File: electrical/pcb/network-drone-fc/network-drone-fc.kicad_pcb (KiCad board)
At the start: 4 copper layers, 36 x 36 mm, 94 parts, among them J1 U.FL-R-SMT-1, J2 TYPE-C 16PIN 2MD, J3 U.FL GPS, J4 ESC, J5 I2C port, J7 Charging board, U1 ESP32-S3FN8, U2 USBLC6-2SC6, U3 AP63205WU-7, U4 TLV75733PDBVR, U5 TPS7A2033PDBVR, U6 ICM-42688-P, U7 BMP581, U8 MAX-M10S, X1 Q22FA12800101

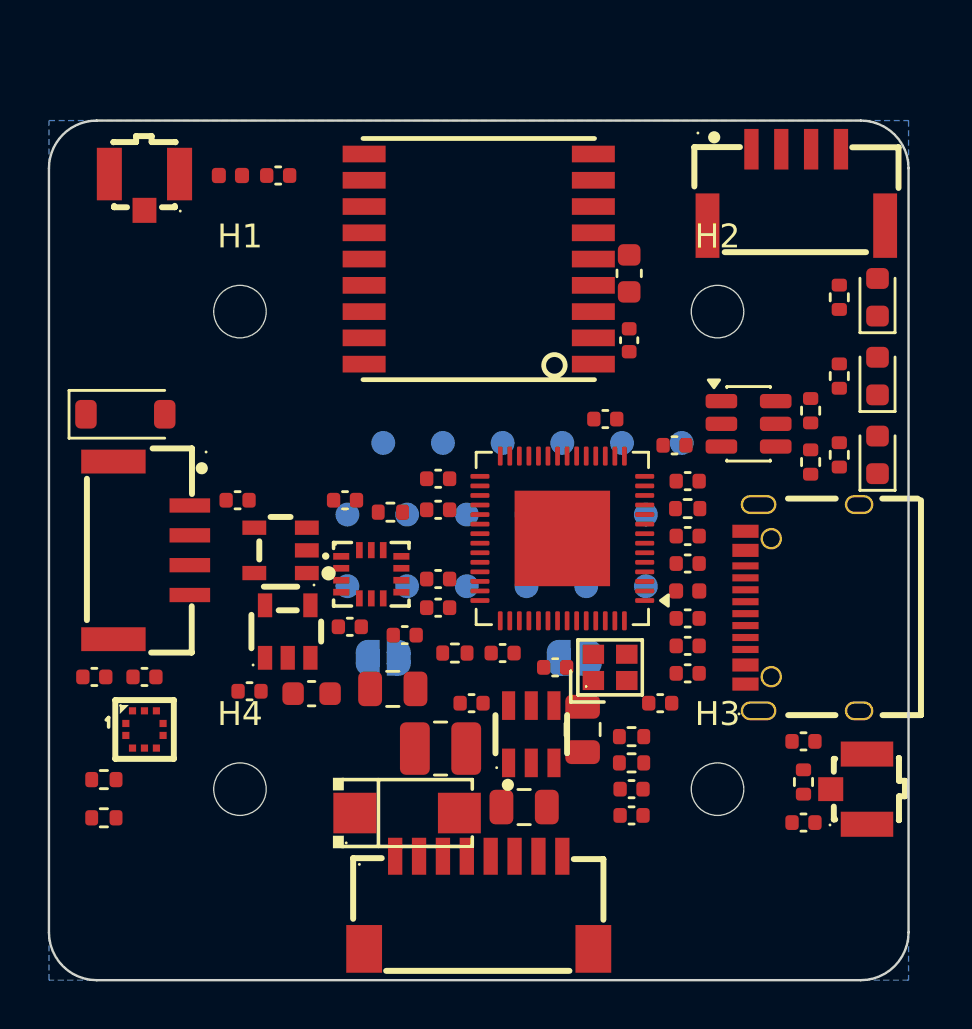
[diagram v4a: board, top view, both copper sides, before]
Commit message: PCB: tighten the buck loop (L2 flipped toward SW, C18 at the inductor output), fix the charging port orientation
The earlier text-level rotation double-rotated J7, L2 and C18 (KiCad stores pad
positions unrotated and applies the footprint angle on load). Corrected, so the
charging port's cable mouth now faces the top edge.
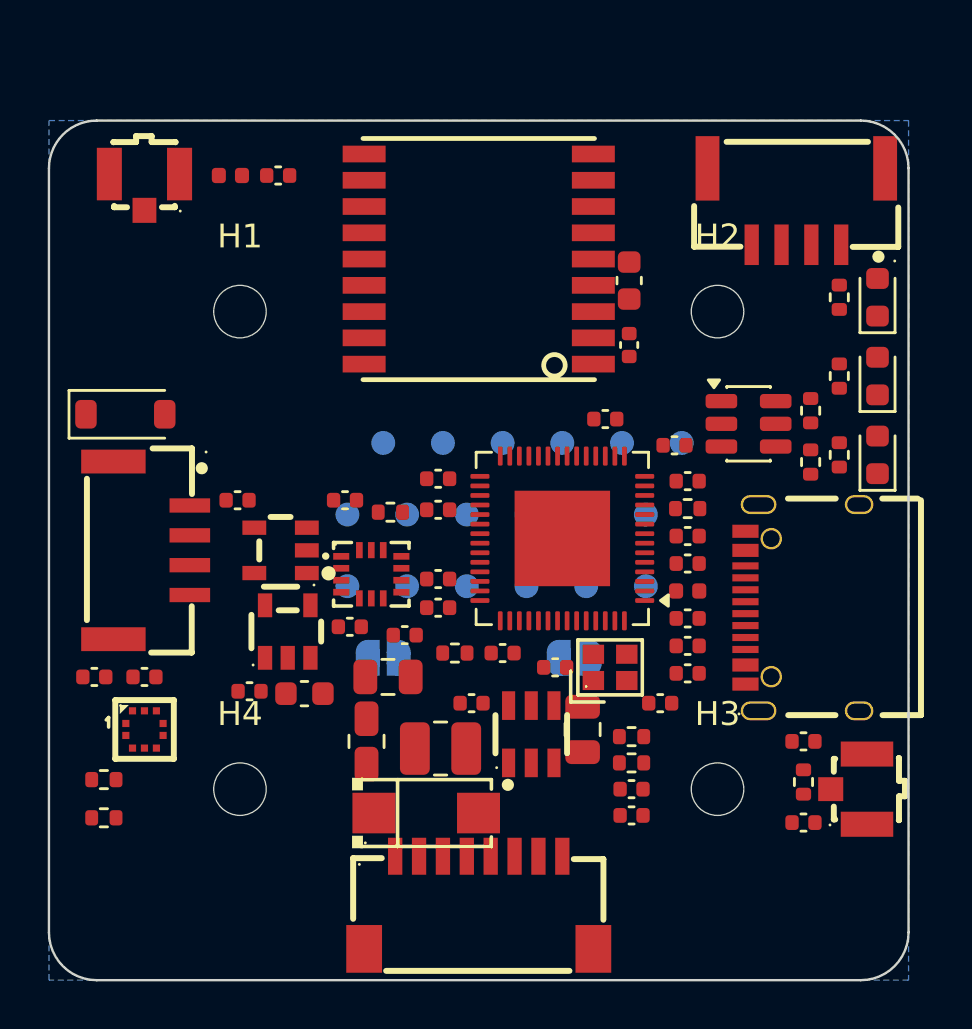
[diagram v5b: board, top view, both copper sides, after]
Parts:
- moved C18 7.15 mm to (95.3, 108.0), turned to 90 degrees
- moved D5 0.80 mm to (97.8, 111.0)
- moved J7 0.80 mm to (113.3, 85.6)
- moved C19 0.54 mm to (96.2, 105.3)
- moved C30 0.30 mm to (106.3, 88.7)
- moved C4 0.30 mm to (92.7, 106.0)
- moved C31 0.20 mm to (106.3, 91.4)
- turned L2 to 180 degrees
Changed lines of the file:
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@@
 	(footprint "SMA_L4.4-W2.6-LS5.0-RD"
 		(layer "F.Cu")
-		(at 97 111)
+		(at 97.8 111.0)
 		(property "Reference" "D5"
 			(at 0 0 0)
@@
 	(footprint "CONN-SMD_4P-P1.25_SM04B-GHS-TB-LF-SN"
 		(layer "F.Cu")
-		(at 113.3 84.8 180)
+		(at 113.3 85.6 180)
 		(property "Reference" "J7"
-			(at 0 0 180)
+			(at -0 0 180)
 			(layer "F.Fab")
 			(effects
@@
 		)
 		(property "Value" "Charging board"
-			(at 0 -5.6 180)
+			(at 0 5.6 180)
 			(layer "F.Fab")
 			(hide yes)
@@
 		)
 		(property "Datasheet" ""
-			(at 0 0 180)
+			(at -0 0 180)
 			(layer "F.Fab")
 			(hide yes)
@@
 		)
 		(property "Description" ""
-			(at 0 0 180)
+			(at -0 0 180)
 			(layer "F.Fab")
 			(hide yes)
@@
 		)
 		(property "LCSC Part" "C189895"
-			(at 0 0 180)
+			(at -0 0 180)
 			(layer "F.Fab")
 			(hide yes)
@@
 		(attr smd)
 		(fp_line
-			(start 4.27 1.69)
-			(end 4.27 0.04)
+			(start -4.27 -1.69)
+			(end -4.27 -0.04)
 			(stroke
 				(width 0.25)
@@
 		)
 		(fp_line
-			(start 3 -2.71)
-			(end -2.92 -2.71)
+			(start -3 2.71)
+			(end 2.92 2.71)
 			(stroke
 				(width 0.25)
@@
 		)
 		(fp_line
-			(start 2.36 1.69)
-			(end 4.27 1.69)
+			(start -2.36 -1.69)
+			(end -4.27 -1.69)
 			(stroke
 				(width 0.25)
@@
 		)
 		(fp_line
-			(start -2.34 1.68)
-			(end -4.28 1.68)
+			(start 2.34 -1.68)
+			(end 4.28 -1.68)
 			(stroke
 				(width 0.25)
@@
 		)
 		(fp_line
-			(start -4.28 1.68)
-			(end -4.28 -0.02)
+			(start 4.28 -1.68)
+			(end 4.28 0.02)
 			(stroke
 				(width 0.25)
@@
 		)
 		(fp_circle
-			(center 4.12 2.28)
-			(end 4.09 2.28)
+			(center -4.12 -2.28)
+			(end -4.09 -2.28)
 			(stroke
 				(width 0.06)
@@
 		)
 		(fp_circle
-			(center 3.44 2.1)
-			(end 3.31 2.1)
+			(center -3.44 -2.1)
+			(end -3.31 -2.1)
 			(stroke
 				(width 0.25)
@@
 		)
 		(fp_circle
-			(center 1.89 1.13)
-			(end 1.76 1.13)
+			(center -1.89 -1.13)
+			(end -1.76 -1.13)
 			(stroke
 				(width 0.25)
@@
 		)
 		(fp_line
-			(start 4.12 1.48)
-			(end -4.13 1.48)
+			(start -4.12 -1.48)
+			(end 4.13 -1.48)
 			(stroke
 				(width 0.05)
@@
 		)
 		(fp_line
-			(start 4.12 -2.57)
-			(end 4.12 1.48)
+			(start -4.12 2.57)
+			(end -4.12 -1.48)
 			(stroke
 				(width 0.05)
@@
 		)
 		(fp_line
-			(start -4.13 1.48)
-			(end -4.13 -2.57)
+			(start 4.13 -1.48)
+			(end 4.13 2.57)
 			(stroke
 				(width 0.05)
@@
 		)
 		(fp_line
-			(start -4.13 -2.57)
-			(end 4.12 -2.57)
+			(start 4.13 2.57)
+			(end -4.12 2.57)
 			(stroke
 				(width 0.05)
@@
 		)
 		(fp_text user "${REFERENCE}"
-			(at 0 0 180)
+			(at -0 0 180)
 			(layer "F.Fab")
 			(effects
@@
 		)
 		(pad "1" smd rect
-			(at 1.88 1.6)
+			(at -1.88 -1.6)
 			(size 0.6 1.7)
 			(layers "F.Cu" "F.Mask" "F.Paste")
@@
 		)
 		(pad "2" smd rect
-			(at 0.63 1.6)
+			(at -0.63 -1.6)
 			(size 0.6 1.7)
 			(layers "F.Cu" "F.Mask" "F.Paste")
@@
 		)
 		(pad "3" smd rect
-			(at -0.62 1.6)
+			(at 0.62 -1.6)
 			(size 0.6 1.7)
 			(layers "F.Cu" "F.Mask" "F.Paste")
@@
 		)
 		(pad "4" smd rect
-			(at -1.87 1.6)
+			(at 1.87 -1.6)
 			(size 0.6 1.7)
 			(layers "F.Cu" "F.Mask" "F.Paste")
 		)
 		(pad "5" smd rect
-			(at -3.72 -1.6)
+			(at 3.72 1.6)
 			(size 1 2.7)
 			(layers "F.Cu" "F.Mask" "F.Paste")
 		)
 		(pad "6" smd rect
-			(at 3.72 -1.6)
+			(at -3.72 1.6)
 			(size 1 2.7)
 			(layers "F.Cu" "F.Mask" "F.Paste")
@@
 	(footprint "L_1008_2520Metric"
 		(layer "F.Cu")
-		(at 98.4 108.3)
+		(at 98.4 108.3 180)
 		(descr "Inductor SMD 1008 (2520 Metric), square (rectangular) end terminal, IPC-7351 nominal, (Body size source: https://ecsxtal.com/store/pdf/ECS-MPI2520-SMD-POWER-INDUCTOR.pdf), generated with kicad-footprint-generator")
 		(tags "inductor")
 		(property "Reference" "L2"
-			(at 0 0 0)
+			(at 0 -0 180)
 			(layer "F.Fab")
 			(effects
@@
 		)
 		(property "Value" "4.7uH"
-			(at 0 2.05 0)
+			(at 0 2.05 180)
 			(layer "F.Fab")
 			(hide yes)
@@
 		)
 		(property "Datasheet" ""
-			(at 0 0 0)
+			(at 0 -0 180)
 			(layer "F.Fab")
 			(hide yes)
@@
 		)
 		(property "Description" ""
-			(at 0 0 0)
+			(at 0 -0 180)
 			(layer "F.Fab")
 			(hide yes)
@@
 		(attr smd)
 		(fp_line
-			(start -0.261252 -1.11)
-			(end 0.261252 -1.11)
+			(start -0.2613 -1.11)
+			(end 0.2613 -1.11)
 			(stroke
 				(width 0.12)
@@
 		)
 		(fp_line
-			(start -0.261252 1.11)
-			(end 0.261252 1.11)
+			(start -0.2613 1.11)
+			(end 0.2613 1.11)
 			(stroke
 				(width 0.12)
@@
 		)
 		(fp_text user "${REFERENCE}"
-			(at 0 0 0)
+			(at 0 -0 180)
 			(layer "F.Fab")
 			(effects
@@
 		)
 		(pad "2" smd roundrect
-			(at 1.075 0)
+			(at 1.075 -0)
 			(size 1.25 2.2)
 			(layers "F.Cu" "F.Mask" "F.Paste")
@@
 	(footprint "C_0805_2012Metric"
 		(layer "F.Cu")
-		(at 101.9 110.75)
+		(at 95.3 108.0 90)
 		(descr "Capacitor SMD 0805 (2012 Metric), square (rectangular) end terminal, IPC-7351 nominal, (Body size source: IPC-SM-782 page 76, https://www.pcb-3d.com/wordpress/wp-content/uploads/ipc-sm-782a_amendment_1_and_2.pdf, https://docs.google.com/spreadsheets/d/1BsfQQcO9C6DZCsRaXUlFlo91Tg2WpOkGARC1WS5S8t0/edit?usp=sharing), generated with kicad-footprint-generator")
 		(tags "capacitor")
 		(property "Reference" "C18"
-			(at 0 0 0)
+			(at 0 0 90)
 			(layer "F.Fab")
 			(effects
@@
 		)
 		(property "Value" "22uF 10V"
-			(at 0 1.68 0)
+			(at 0 1.68 90)
 			(layer "F.Fab")
 			(hide yes)
@@
 		)
 		(property "Datasheet" ""
-			(at 0 0 0)
+			(at 0 0 90)
 			(layer "F.Fab")
 			(hide yes)
@@
 		)
 		(property "Description" ""
-			(at 0 0 0)
+			(at 0 0 90)
 			(layer "F.Fab")
 			(hide yes)
@@
 		(attr smd)
 		(fp_line
-			(start -0.261252 -0.735)
-			(end 0.261252 -0.735)
+			(start -0.2613 -0.735)
+			(end 0.2613 -0.735)
 			(stroke
 				(width 0.12)
@@
 		)
 		(fp_line
-			(start -0.261252 0.735)
-			(end 0.261252 0.735)
+			(start -0.2613 0.735)
+			(end 0.2613 0.735)
 			(stroke
 				(width 0.12)
@@
 		)
 		(fp_text user "${REFERENCE}"
-			(at 0 0 0)
+			(at 0 0 90)
 			(layer "F.Fab")
 			(effects
@@
 	(footprint "C_0805_2012Metric"
 		(layer "F.Cu")
-		(at 96.4 105.8)
+		(at 96.2 105.3)
 		(descr "Capacitor SMD 0805 (2012 Metric), square (rectangular) end terminal, IPC-7351 nominal, (Body size source: IPC-SM-782 page 76, https://www.pcb-3d.com/wordpress/wp-content/uploads/ipc-sm-782a_amendment_1_and_2.pdf, https://docs.google.com/spreadsheets/d/1BsfQQcO9C6DZCsRaXUlFlo91Tg2WpOkGARC1WS5S8t0/edit?usp=sharing), generated with kicad-footprint-generator")
 		(tags "capacitor")
@@
 	(footprint "C_0603_1608Metric"
 		(layer "F.Cu")
-		(at 106.3 88.4 90)
+		(at 106.3 88.7 90)
 		(descr "Capacitor SMD 0603 (1608 Metric), square (rectangular) end terminal, IPC-7351 nominal, (Body size source: IPC-SM-782 page 76, https://www.pcb-3d.com/wordpress/wp-content/uploads/ipc-sm-782a_amendment_1_and_2.pdf), generated with kicad-footprint-generator")
 		(tags "capacitor")
@@
 	(footprint "C_0603_1608Metric"
 		(layer "F.Cu")
-		(at 93 106)
+		(at 92.7 106.0)
 		(descr "Capacitor SMD 0603 (1608 Metric), square (rectangular) end terminal, IPC-7351 nominal, (Body size source: IPC-SM-782 page 76, https://www.pcb-3d.com/wordpress/wp-content/uploads/ipc-sm-782a_amendment_1_and_2.pdf), generated with kicad-footprint-generator")
 		(tags "capacitor")
@@
 	(footprint "C_0402_1005Metric"
 		(layer "F.Cu")
-		(at 106.3 91.2 90)
+		(at 106.3 91.4 90)
 		(descr "Capacitor SMD 0402 (1005 Metric), square (rectangular) end terminal, IPC-7351 nominal, (Body size source: IPC-SM-782 page 76, https://www.pcb-3d.com/wordpress/wp-content/uploads/ipc-sm-782a_amendment_1_and_2.pdf), generated with kicad-footprint-generator")
 		(tags "capacitor")

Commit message: PCB: charging port clear of the corner arc
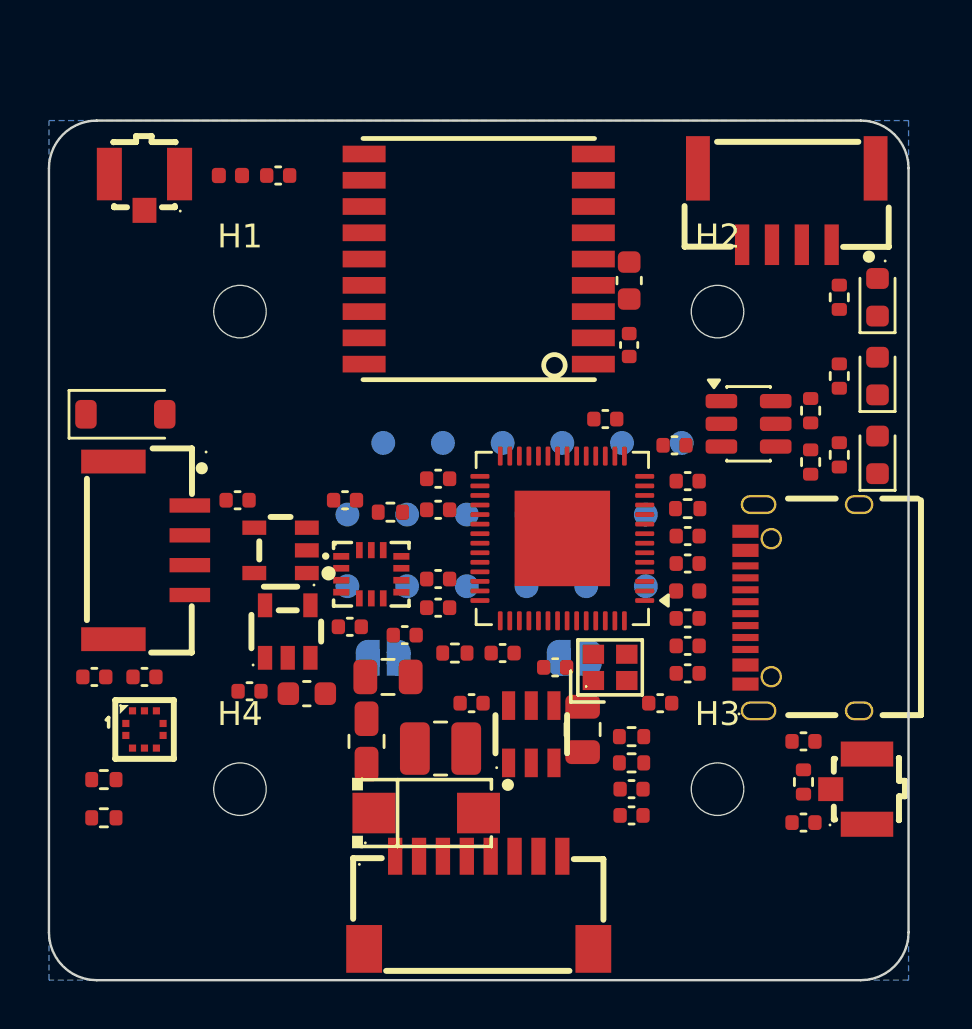
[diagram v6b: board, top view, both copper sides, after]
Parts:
- moved J7 0.40 mm to (112.9, 85.6)
- moved C4 0.10 mm to (92.8, 106.0)
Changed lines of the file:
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@@
 	(footprint "CONN-SMD_4P-P1.25_SM04B-GHS-TB-LF-SN"
 		(layer "F.Cu")
-		(at 113.3 85.6 180)
+		(at 112.9 85.6 180)
 		(property "Reference" "J7"
 			(at -0 0 180)
@@
 	(footprint "C_0603_1608Metric"
 		(layer "F.Cu")
-		(at 92.7 106.0)
+		(at 92.8 106.0)
 		(descr "Capacitor SMD 0603 (1608 Metric), square (rectangular) end terminal, IPC-7351 nominal, (Body size source: IPC-SM-782 page 76, https://www.pcb-3d.com/wordpress/wp-content/uploads/ipc-sm-782a_amendment_1_and_2.pdf), generated with kicad-footprint-generator")
 		(tags "capacitor")

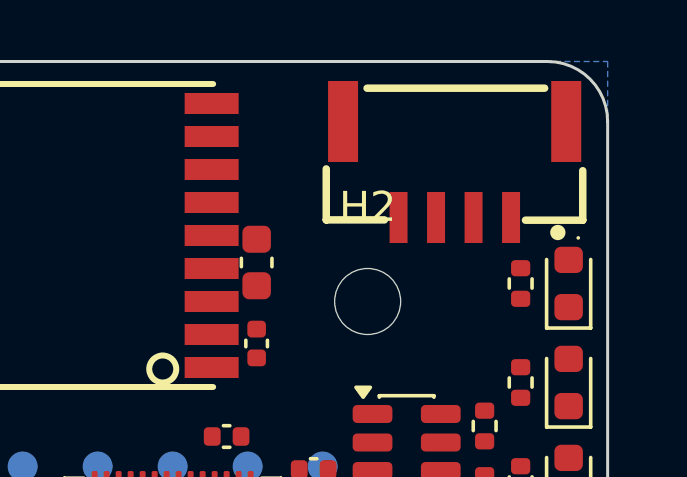
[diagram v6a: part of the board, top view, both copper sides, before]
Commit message: PCB: charging port 0.3 mm from the corner arc
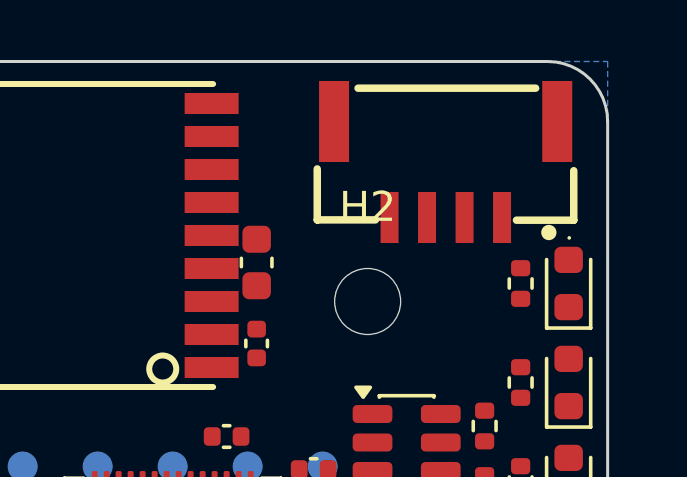
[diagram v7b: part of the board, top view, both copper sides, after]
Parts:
- moved J7 0.30 mm to (112.6, 85.6)
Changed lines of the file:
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@@
 	(footprint "CONN-SMD_4P-P1.25_SM04B-GHS-TB-LF-SN"
 		(layer "F.Cu")
-		(at 112.9 85.6 180)
+		(at 112.6 85.6 180)
 		(property "Reference" "J7"
 			(at -0 0 180)
